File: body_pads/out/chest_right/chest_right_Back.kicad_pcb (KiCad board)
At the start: 2 copper layers, 165.5 x 206.5 mm, 0 parts

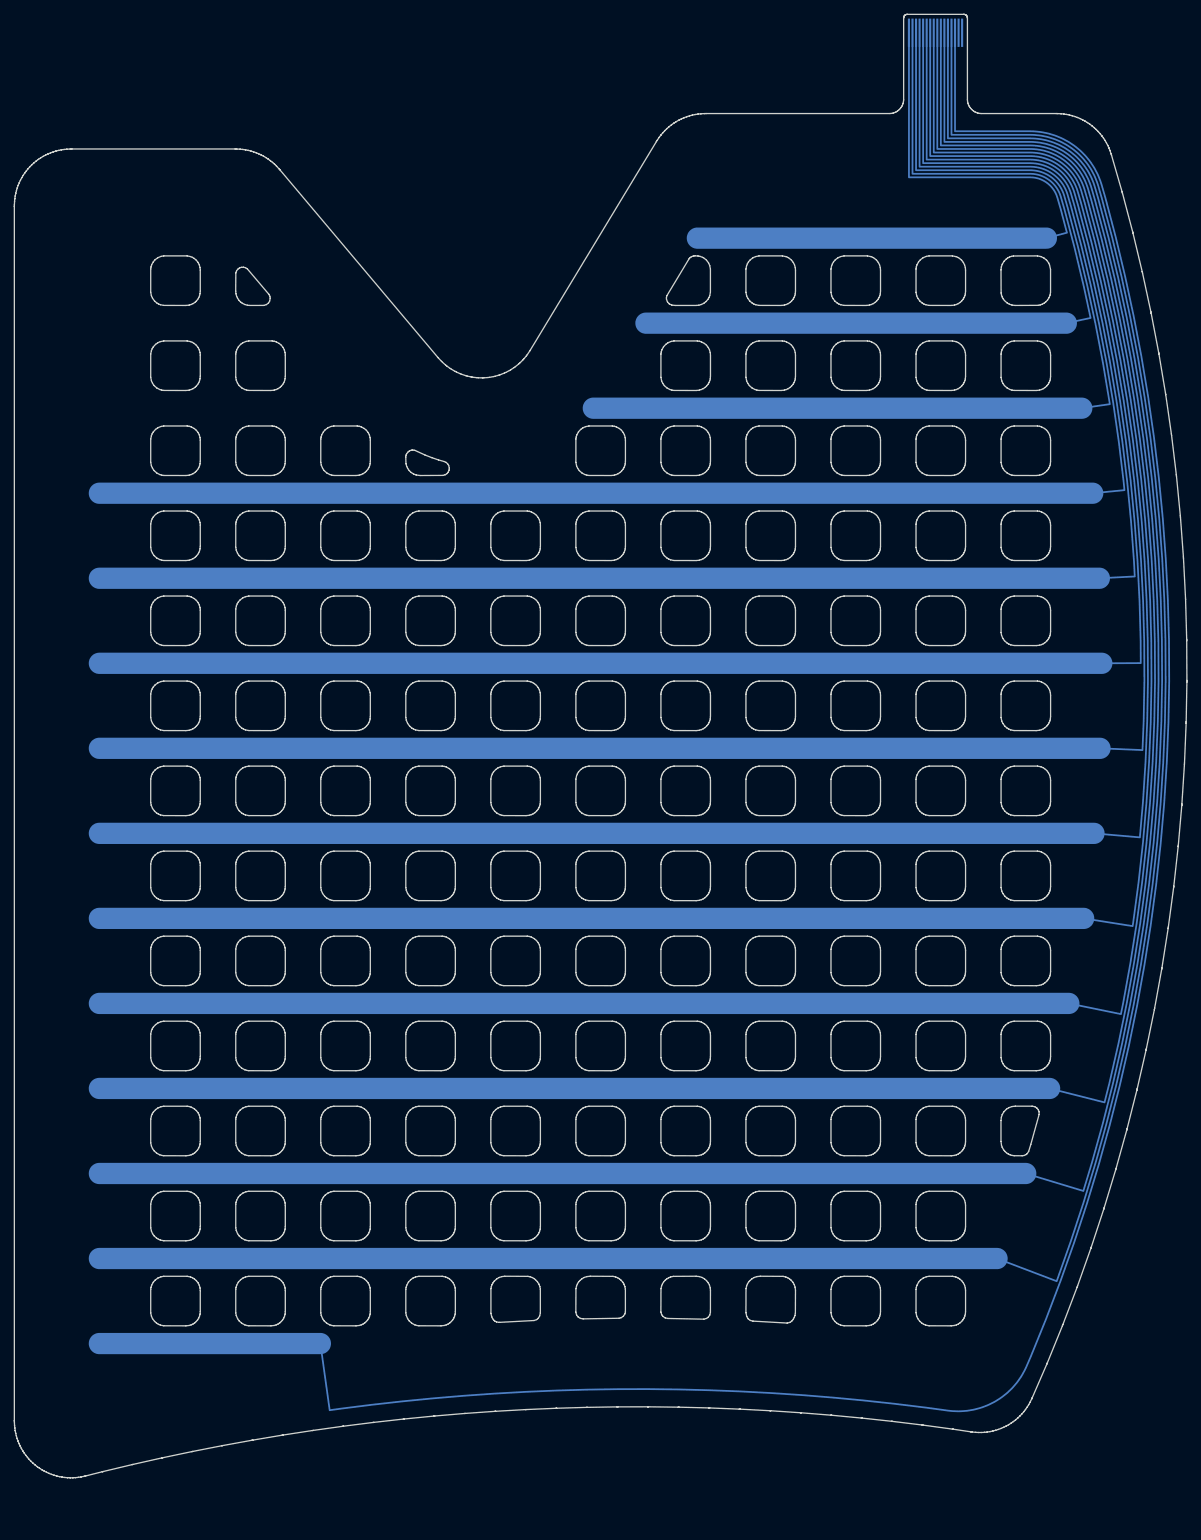
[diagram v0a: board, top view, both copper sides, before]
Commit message: Terminate body pads with vias and an FFC connector; export the full Gerber set
The pad tails now follow README Step 5 like the glove: every electrode trace
ends in a through via (0.45/0.2 mm, two staggered rows) and a 16-pin 0.5 mm
FFC connector (KiCad library Hirose FH12-16S-0.5SH) sits on the side opposite
the electrodes, making each board a 2-layer flex. A nested staircase fans the
0.5 mm bus out to the 1.0 mm via pitch and back to the 0.5 mm pads without
crossings. body_pads/kicad_post.py runs with KiCad's own python to add the
vias, footprint, connector-side tracks and nets; a .kicad_pro with flex rules
is written so kicad-cli DRC checks the right limits, and the Gerber export now
produces the same file set as the glove (both copper layers, mask, paste,
silkscreen, edge cuts, Eco1/Eco2, PTH/NPTH drills and maps).

Also: the column grid is shifted so no column exits under the tail bus, the
mirrored chest half swaps its tail order so both halves match, previews gain
a tail close-up, and the README describes the new tail, layers and checks.
Includes the body-pad documentation docx added to the working tree.

Co-Authored-By: Claude Fable 5.1 <noreply@anthropic.com>
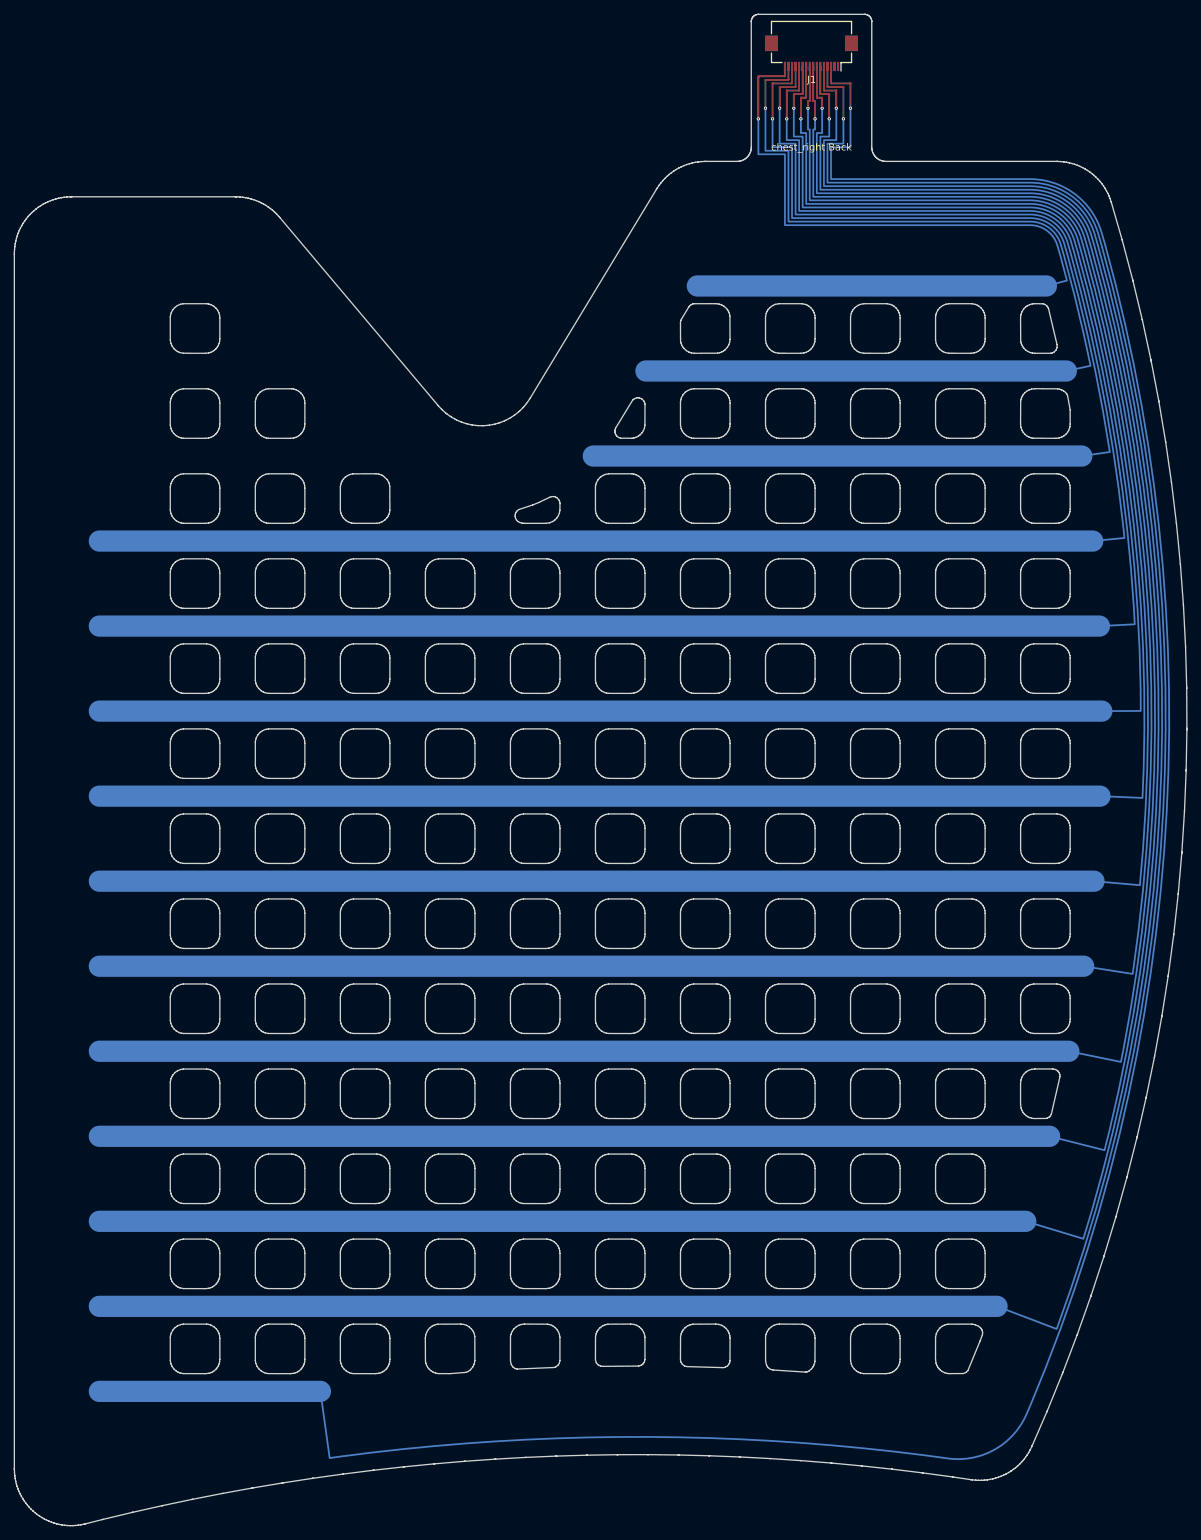
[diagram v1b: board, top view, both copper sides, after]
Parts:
- added J1: Hirose_FH12-16S-0.5SH_1x16-1MP_P0.50mm_Horizontal, Hirose_FH12-16S-0.5SH_1x16-1MP_P0.50mm_Horizontal, F.Cu at (122.5, 15.5)
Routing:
- net ROW13: track 0.00 -> 11.2 mm, vias 0 -> 1
- net ROW11: track 0.00 -> 10.2 mm, vias 0 -> 1
- net ROW01: track 0.00 -> 9.65 mm, vias 0 -> 1
- net ROW12: track 0.00 -> 9.15 mm, vias 0 -> 1
- net ROW09: track 0.00 -> 9.15 mm, vias 0 -> 1
- net ROW03: track 0.00 -> 8.65 mm, vias 0 -> 1
- net ROW00: track 0.00 -> 8.65 mm, vias 0 -> 1
- net ROW10: track 0.00 -> 8.15 mm, vias 0 -> 1
- net ROW07: track 0.00 -> 8.15 mm, vias 0 -> 1
- net ROW05: track 0.00 -> 7.65 mm, vias 0 -> 1
- net ROW02: track 0.00 -> 7.65 mm, vias 0 -> 1
- net ROW08: track 0.00 -> 7.15 mm, vias 0 -> 1
- net ROW04: track 0.00 -> 6.65 mm, vias 0 -> 1
- net ROW06: track 0.00 -> 6.15 mm, vias 0 -> 1
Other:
- board size 165.5 x 206.5 mm -> 165.5 x 213.3 mm
- board text added: "chest_right Back"
- board text added: "chest_right Back: 2-layer flex. Electrodes on B.Cu under the B.Mask opening; FFC connector J1 on F.Cu. Eco1.User = PSA adhesive on the B.Cu side. Eco2.User = stiffener under the connector (on the B.Cu side of the tail)."
- board text removed: "chest_right Back: 1-layer flex, copper on B.Cu. B.Mask = coverlay openings. Eco1.User = PSA adhesive (copper side). Eco2.User = tail stiffener (opposite side), total tail 0.30 +/-0.05 mm. 16-pin 0.5 mm FFC fingers."
